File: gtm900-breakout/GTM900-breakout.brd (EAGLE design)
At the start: 70 x 70 mm, 45 parts, among them K1 694108106102, T1 BC847, U1 FH12A-40S-0.5SH(55), U2 FH12A-40S-0.5SH(55), U3 MCP1827T-ADJE/ET

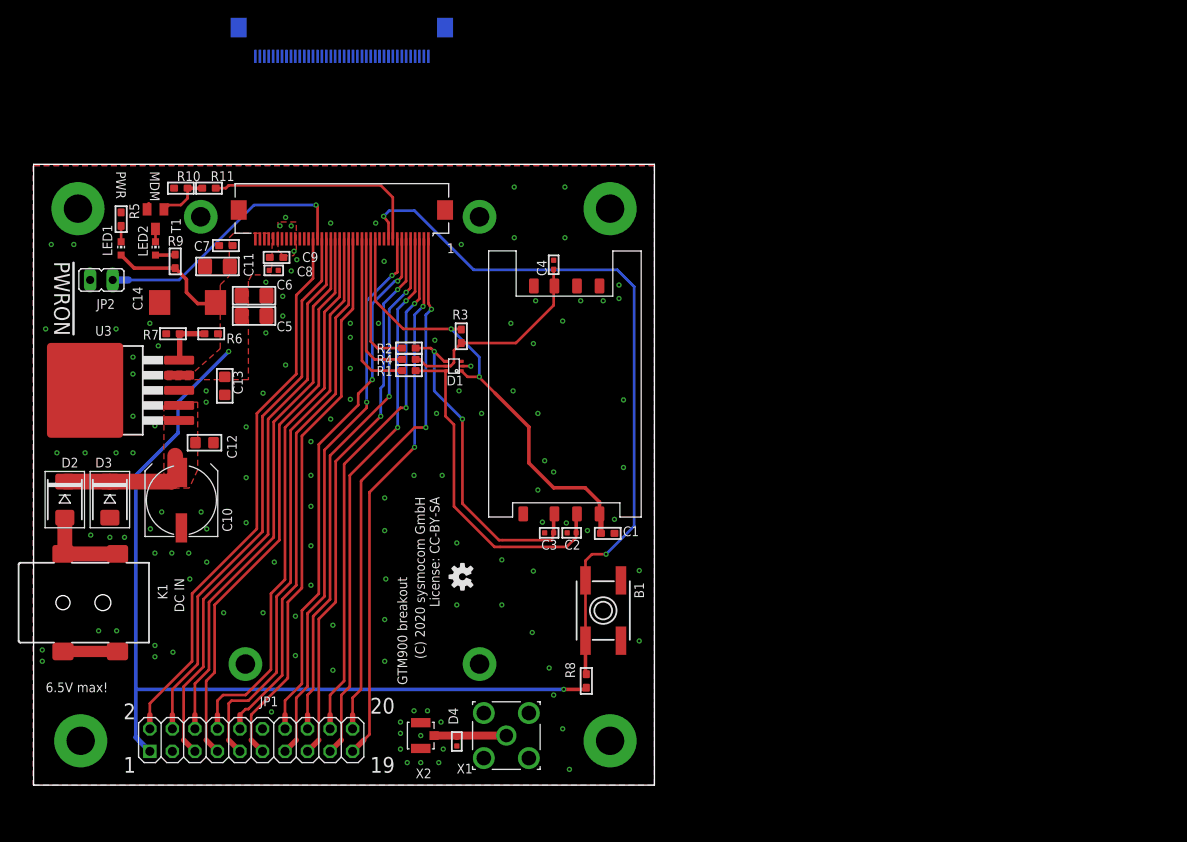
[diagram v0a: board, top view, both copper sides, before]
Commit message: gtm900: added CP2105 and 3.5mm TRRS audio jack, remv'd aux conn
adds to OS#4030
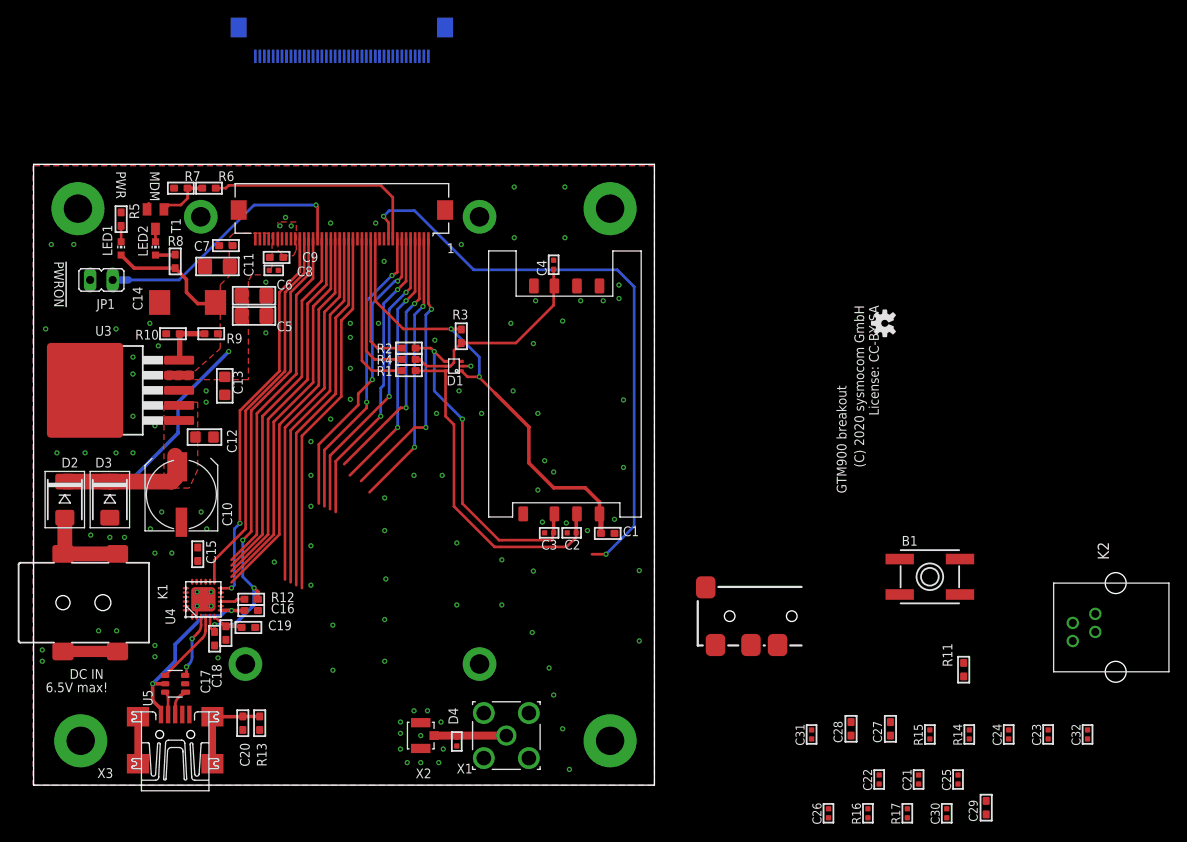
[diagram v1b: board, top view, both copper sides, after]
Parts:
- removed JP2: (no value), jumper:JP1
- added C15, C19: 4.7u, rc-sysmocom:_0603
- added C16: 1u, rc-sysmocom:_0603
- added C17, C18, C20, C27, C28: 100n, rc-sysmocom:_0603
- added C21, C22, C23, C24, C25, C26, C30, C31, C32: 33p, rc-sysmocom:_0402
- added C29: 22u, rc-sysmocom:_0603
- added J1: SJ2-3574A, SparkFun-Connectors:AUDIO-JACK-TRRS-SMD
- added K2: 615004143821, Wuerth_Elektronik_eiCan_Communication_Connectors_v6_20150113:615004143821
- added R12: 4.7k, rc-sysmocom:_0603@1
- added R13: 1M, rc-sysmocom:_0603@1
- added R14, R17: 100, rc-sysmocom:_0402@1
- added R15, R16: 2.2k, rc-sysmocom:_0402@1
- added U4: CP2105-GM, usb-uart:QFN24_4X4
- added U5: IP4234CZ6, laforge:TSOP-6
- added X3: MINI-USB-SHIELD-UX60-MB-5ST, con-hirose:UX60-MB-5ST
- JP1: device laforge:2X10 -> jumper:JP1
- R1, R10, R2, R3, R4, R5, R7: device rc-sysmocom:_0603 -> rc-sysmocom:_0603@1
- R11: value 22k -> 15k; device rc-sysmocom:_0603 -> rc-sysmocom:_0603@1
- R6: value 200k -> 22k; device rc-sysmocom:_0603 -> rc-sysmocom:_0603@1
- R8: value 15k -> 330; device rc-sysmocom:_0603 -> rc-sysmocom:_0603@1
- R9: value 330 -> 200k; device rc-sysmocom:_0603 -> rc-sysmocom:_0603@1
- moved R11 100.9 mm to (78.7, 13.0), turned to 90 degrees
- moved R8 66.2 mm to (-10.2, 59.1)
- moved U$1 55.5 mm to (69.8, 52.1)
- moved JP1 54.6 mm to (-18.5, 57.0), turned to 90 degrees
- moved B1 37.0 mm to (74.9, 23.5), turned to 0 degrees
- moved R10 16.4 mm to (-10.4, 50.9)
- moved R7 16.4 mm to (-9.53, 67.3)
- moved R6 16.4 mm to (-6.35, 67.3), turned to 180 degrees
- moved R9 9.12 mm to (-6.10, 50.9), turned to 0 degrees
- moved C12 0.64 mm to (-6.86, 39.2)
- moved C10 0.63 mm to (-9.46, 32.8)
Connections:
- removed net N$24: JP1.12
- new net N$11: C20.2, R13.2, X3.M1, X3.M2, X3.M3, X3.M4
- new net N$12: R12.1, U4.9
- new net N$14: C15.2, U4.16
- new net N$15: C27.2, C31.1, J1.RING2, R15.2
- new net N$16: C29.1, C30.1, R14.2, R15.1
- new net N$17: C29.2, C30.2, R16.2, R17.1
- new net N$20: C28.2, C31.2, J1.TIP, R16.1
- new net USB_DN: U4.4, U5.4
- new net USB_DP: U4.3, U5.3
- new net USB_VBUS: C16.1, U4.7, U4.8, U5.5, X3.1
- new net VDD_3V45: C18.1, C19.1, U4.6
- new net _USB_DN: U5.6, X3.2
- new net _USB_DP: U5.1, X3.3
- net !RST: now also R11.2; no longer R8.2
- net ADC: no longer JP1.2
- net AUXI+: no longer JP1.19
- net AUXI-: no longer JP1.20
- net AUXO+: no longer JP1.13
- net AUXO-: no longer JP1.14
- net EAR+: now also C23.1, C26.1, C32.2, J1.RING1; no longer JP1.15
- net EAR-: now also C24.2, C26.2, C32.1, J1.EARTH; no longer JP1.16
- net GND: now also C15.1, C16.2, C17.1, C18.2, C19.2, C20.1, C21.2, C22.1, C23.2, C24.1, JP1.2, R13.1, R17.2, U4.2, U4.25, U5.2, X3.5; no longer JP1.3, JP2.2
- net LPG: now also R6.1; no longer R11.1
- net MIC+: now also C21.1, C25.1, C27.1; no longer JP1.17
- net MIC-: now also C22.2, C25.2, C28.1; no longer JP1.18
- net N$2: now also R8.2; no longer R9.2
- net N$5: now also R6.2, R7.1; no longer R10.1, R11.2
- net N$6: now also R10.1, R9.1; no longer R6.1, R7.1
- net PWON: now also JP1.1; no longer JP2.1
- net RXD2: now also U4.12
- net TXD2: now also U4.13
- net UART_CTS: now also U4.18; no longer JP1.8
- net UART_DCD: now also U4.24; no longer JP1.11
- net UART_DSR: now also U4.22; no longer JP1.4
- net UART_DTR: now also U4.23; no longer JP1.10
- net UART_RI: now also U4.1; no longer JP1.5
- net UART_RTS: now also U4.19; no longer JP1.9
- net UART_RXD: now also U4.20; no longer JP1.6
- net UART_TXD: now also U4.21; no longer JP1.7
- net VCC: now also R11.1, R9.2; no longer JP1.1, R6.2, R9.1
- net VDD: now also C17.2, R12.2, R14.1, U4.5
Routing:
- net VCC: track 114.8 -> 32.1 mm, vias 2 -> 1
- net VDD: track 0.00 -> 54.4 mm, vias 0 -> 3
- net RXD2: track 0.00 -> 43.8 mm, vias 0 -> 2
- net TXD2: track 0.00 -> 42.9 mm
- net MIC+: track 61.8 -> 29.7 mm
- net MIC-: track 59.8 -> 29.3 mm
- net AUXI+: track 61.1 -> 31.1 mm
- net AUXO+: track 63.1 -> 33.7 mm
- net AUXI-: track 59.8 -> 31.4 mm
- net EAR+: track 62.4 -> 34.1 mm
- net AUXO-: track 60.9 -> 33.9 mm
- net EAR-: track 60.1 -> 34.2 mm
- net UART_RTS: track 64.8 -> 41.2 mm
- net UART_RI: track 65.0 -> 41.9 mm
- net ADC: track 62.9 -> 40.0 mm
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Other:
- board text removed: "19"
- board text removed: "2"
- board text removed: "20"

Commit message: gtm900-bo: hopefully incorporating all we discussed last weeks
see OS#4030
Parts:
- removed K2: 615004143821, Wuerth_Elektronik_eiCan_Communication_Connectors_v6_20150113:615004143821
- removed U$1: (no value), SparkFun-Aesthetics:OSHW-LOGO-S
- added B2: (no value), microbuilder:EVQ-Q2
- added C33, C34: 33p, rc-sysmocom:_0402
- added D5: PESD5V0UBV, laforge:SOT666
- added JP2: (no value), microbuilder:1X04_ROUND_76
- added LOGO3: OSHW-LOGOS-COPPER, SparkFun-Aesthetics:OSHW-LOGO-S_COPPER
- added R18, R20, R21: 22k, rc-sysmocom:_0603@1
- added R19: 330, rc-sysmocom:_0603@1
- added R22: DNP, rc-sysmocom:_0603@1
- added R23: 1k, rc-sysmocom:_0603@1
- added R24: 4.7k, rc-sysmocom:_0603@1
- added R25: 1M, rc-sysmocom:_0603@1
- added R26: 0, rc-sysmocom:_0603@1
- added T2, T3, T4: BC847, transistor:SOT23-BEC
- added TP1, TP2, TP3, TP4, TP5: TPTP10R, testpad:TP10R
- added U$3: (no value), SparkFun-Aesthetics:OSHW-LOGO-S
- added U6: IP4234CZ6, laforge:TSOP-6
- added X4: MINI-USB-SHIELD-UX60-MB-5ST, con-hirose:UX60-MB-5ST
- C10: value 470u -> 100u; device rcl:UD-8X10_NICHICON -> rc-sysmocom:1206
- C11: value 100u -> 470u; device rc-sysmocom:1206 -> rcl:UD-8X10_NICHICON
- C13: value 10u -> 100n; device rc-sysmocom:_0805 -> rc-sysmocom:_0603
- C14: value DNP -> 1u; device rcl:SMC_E -> rc-sysmocom:_0603
- C15: value 4.7u -> 1u
- C16: value 1u -> 10u; device rc-sysmocom:_0603 -> rc-sysmocom:_0805
- C17: value 100n -> DNP; device rc-sysmocom:_0603 -> rcl:SMC_E
- C20: value 100n -> 1u
- C21, C22, C24: value 33p -> 100n; device rc-sysmocom:_0402 -> rc-sysmocom:_0603
- C23: value 33p -> 4.7u; device rc-sysmocom:_0402 -> rc-sysmocom:_0603
- C27, C28: value 100n -> 33p; device rc-sysmocom:_0603 -> rc-sysmocom:_0402
- C29: value 22u -> 33p; device rc-sysmocom:_0603 -> rc-sysmocom:_0402
- C31, C32: value 33p -> 10u; device rc-sysmocom:_0402 -> rc-sysmocom:_0805
- J1: value SJ2-3574A -> AUDIO-JACK3
- MDM1: value GTM900-B -> GTM900-BM2-SPACER; device GTM900:GTM900 -> GTM900:GTM900-WRTHSPACER
- R1: value 47 -> 15k
- R11: value 15k -> 4.7k
- R12: value 4.7k -> DNP
- R13: value 1M -> 1k
- R14: value 100 -> 0; device rc-sysmocom:_0402@1 -> rc-sysmocom:_0603@1
- R15: value 2.2k -> 200k; device rc-sysmocom:_0402@1 -> rc-sysmocom:_0603@1
- R16: value 2.2k -> 22k; device rc-sysmocom:_0402@1 -> rc-sysmocom:_0603@1
- R17: value 100 -> 22k; device rc-sysmocom:_0402@1 -> rc-sysmocom:_0603@1
- R3: value 15k -> 47
- R4: value 47 -> 4.7k
- R5: value 330 -> 47k
- R6: value 22k -> 330
- R8: value 330 -> 22k
- R9: value 200k -> 22k
- U4: value CP2105-GM -> MIC5366; device usb-uart:QFN24_4X4 -> ldo:SC70-5
- U5: value IP4234CZ6 -> CP2105-GM; device laforge:TSOP-6 -> usb-uart:QFN24_4X4
- X1: device laforge:SMA-F-S-TH -> laforge:1X03
- X2: device laforge:HRS_UFL -> laforge:SMA-F-S-TH
- X3: value MINI-USB-SHIELD-UX60-MB-5ST -> (none); device con-hirose:UX60-MB-5ST -> laforge:HRS_UFL
- moved R17 105.7 mm to (-6.35, 67.3), turned to 180 degrees
- moved R16 95.2 mm to (-10.4, 50.9), turned to 180 degrees
- moved R15 92.8 mm to (-6.10, 50.9), turned to 0 degrees
- moved C24 89.6 mm to (-5.71, 10.2), turned to 0 degrees
- moved C23 89.3 mm to (0.00, 19.1), turned to 270 degrees
- moved C32 84.1 mm to (9.53, 18.4)
- moved C25 84.0 mm to (14.3, 55.2), turned to 135 degrees
- moved C29 83.9 mm to (18.0, 52.6), turned to 0 degrees
- moved C30 83.3 mm to (15.9, 53.7), turned to 315 degrees
- moved C21 79.3 mm to (-2.86, 21.3), turned to 0 degrees
- moved T1 73.0 mm to (40.0, 13.0), turned to 0 degrees
- moved C22 72.9 mm to (-1.27, 19.1), turned to 270 degrees
- moved R7 71.8 mm to (35.6, 11.4), turned to 270 degrees
- moved C28 69.0 mm to (14.9, 52.7), turned to 315 degrees
- moved R14 66.7 mm to (17.1, 29.8)
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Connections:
- removed net N$20: C28.2, C31.2, J1.TIP, R16.1
- removed net PWON: JP1.1, U1.26, U2.15
- removed net USB_DN: U4.4, U5.4
- removed net USB_DP: U4.3, U5.3
- removed net _USIM_IO: R4.1, U1.15, U2.26
- new net !PWON: C18.1, JP1.1, R22.2, R23.1, T4.C, U1.26, U2.15
- new net GPIO.0_ECI/DTR_ECI: R14.2, R20.1, U5.15
- new net GPIO.1_ECI/DSR_ECI: R7.1, U5.14
- new net N$10: R4.1, SIM1.82
- new net N$18: R11.1, R14.1, T2.C
- new net N$21: B1.A, B1.A', R13.2
- new net N$7: R10.1, R8.2, T2.B
- new net N$8: C32.1, C34.2, J1.2, J1.3
- new net N$9: B2.A, B2.A', R23.2
- new net USB_D_N: U5.4, U6.4
- new net USB_D_P: U5.3, U6.3
- new net VIO_2V8: C15.2, C21.2, R11.2, R12.1, R22.1, U4.5, U5.5
- net !RST: now also C13.1, R12.2, R13.1, T1.C; no longer B1.A, B1.A', R11.2
- net ADC: now also X1.1
- net AUXI+: now also TP3.TP
- net AUXI-: now also TP5.TP
- net AUXO+: now also TP2.TP
- net AUXO-: now also TP4.TP
- net EAR+: now also C25.2, D5.3, JP2.3; no longer C23.1, J1.RING1
- net EAR-: now also C25.1, C27.2, D5.1, JP2.4, R26.2; no longer C24.2, C26.2, C32.1, J1.EARTH
- net GND: now also B2.B, B2.B', C10.1, C11.-, C13.2, C14.1, C16.1, C17.-, C19.1, C20.2, C21.1, C22.2, C26.2, C27.1, C28.2, C29.2, C31.2, C33.2, C34.1, D5.2, J1.4, MDM1.1, MDM1.2, MDM1.3, MDM1.4, R16.2, R18.2, R21.2, R25.1, R26.1, R6.1, R9.2, T2.E, T3.E, T4.E, U5.25, U6.2, X1.3, X2.G1, X2.G2, X2.G3, X2.G4, X3.GND@1, X3.GND@2, X4.5; no longer C10.-, C11.1, C13.1, C14.-, C16.2, C17.1, C19.2, C20.1, C21.2, C22.1, MDM1.P$1, MDM1.P$2, MDM1.P$3, MDM1.P$4, R13.1, R17.2, R7.2, U4.25, X1.G1, X1.G2, X1.G3, X1.G4, X2.GND@1, X2.GND@2, X3.5
- net LDO_IN: now also C11.+; no longer C10.+
- net LPG: now also R17.1; no longer R6.1
- net MIC+: now also C28.1, C30.1, C33.1, D5.4, J1.1, JP2.1; no longer C21.1, C25.1, C27.1
- net MIC-: now also C29.1, C30.2, C31.1, D5.5, JP2.2; no longer C22.2, C25.2, C28.1
- net N$1: now also R6.2; no longer R5.2
- net N$11: now also C24.2, R25.2, X4.M1, X4.M2, X4.M3, X4.M4; no longer C20.2, R13.2, X3.M1, X3.M2, X3.M3, X3.M4
- net N$12: now also R24.1, U5.9; no longer R12.1, U4.9
- net N$13: now also X2.C, X3.SIG; no longer X1.C, X2.SIG
- net N$14: now also C19.2, U5.16; no longer C15.2, U4.16
- net N$15: now also R4.2; no longer C27.2, C31.1, J1.RING2, R15.2
- net N$16: now also R20.2, R21.1, T4.B; no longer C29.1, C30.1, R14.2, R15.1
- net N$17: now also R7.2, R9.1, T1.B; no longer C29.2, C30.2, R16.2, R17.1
- net N$2: now also R19.2; no longer R8.2
- net N$3: now also T3.C; no longer T1.C
- net N$5: now also R17.2, R18.1, T3.B; no longer R6.2, R7.1, T1.B
- net N$6: now also R15.1, R16.1; no longer R10.1, R9.1
- net RXD2: now also U5.12; no longer U4.12
- net TXD2: now also U5.13; no longer U4.13
- net UART_CTS: now also U5.18; no longer U4.18
- net UART_DCD: now also U5.24; no longer U4.24
- net UART_DSR: now also U5.22; no longer U4.22
- net UART_DTR: now also R8.1, U5.23; no longer U4.23
- net UART_RI: now also U5.1; no longer U4.1
- net UART_RTS: now also U5.19; no longer U4.19
- net UART_RXD: now also U5.20; no longer U4.20
- net UART_TXD: now also U5.21; no longer U4.21
- net USB_VBUS: now also C14.2, C20.1, U4.1, U4.3, U5.7, U5.8, U6.5, X4.1; no longer C16.1, U4.7, U4.8, U5.5, X3.1
- net USIM_CD: now also R5.2, SIM1.81
- net USIM_CLK: now also R3.2; no longer R2.2
- net USIM_IO: now also R1.1, U1.15, U2.26; no longer R3.1, R4.2
- net USIM_RESET: now also R2.2; no longer R1.2
- net USIM_VCC: now also R1.2; no longer R3.2
- net VBACKUP: now also X1.2
- net VCC: now also C10.2, C16.2, C17.+, R15.2, R19.1; no longer C11.2, C13.2, C14.+, R11.1, R8.1, R9.2
- net VDD: now also R24.2; no longer C17.2, R12.2, R14.1, U4.5
- net VDD_3V45: now also C22.1, C23.1, TP1.TP, U5.6; no longer C18.1, C19.1, U4.6
- net _USB_DN: now also U6.6, X4.2; no longer U5.6, X3.2
- net _USB_DP: now also U6.1, X4.3; no longer U5.1, X3.3
- net _USIM_CLK: now also R3.1; no longer R2.1
- net _USIM_RESET: now also R2.1; no longer R1.1
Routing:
- net VIO_2V8: track 0.00 -> 83.5 mm, vias 0 -> 3
- net !PWON: track 0.00 -> 79.1 mm, vias 0 -> 2
- net USIM_CD: track 0.00 -> 45.7 mm, vias 0 -> 3
- net GPIO.1_ECI/DSR_ECI: track 0.00 -> 35.3 mm, vias 0 -> 2
- net PWON: track 30.3 -> 0.00 mm, vias 1 -> 0
- net MIC+: track 29.7 -> 57.9 mm, vias 2 -> 1
- net VBACKUP: track 0.00 -> 26.4 mm, vias 0 -> 1
- net GPIO.0_ECI/DTR_ECI: track 0.00 -> 21.6 mm, vias 0 -> 2
- net USB_VBUS: track 21.8 -> 43.4 mm, vias 2 -> 3
- net USB_D_N: track 0.00 -> 20.0 mm
- net USIM_IO: track 23.7 -> 43.3 mm
- net USB_D_P: track 0.00 -> 19.6 mm, vias 0 -> 2
- net VCC: track 32.1 -> 13.8 mm, vias 1 -> 0
- net _USIM_IO: track 17.1 -> 0.00 mm
- net AUXO-: track 33.9 -> 18.4 mm
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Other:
- board text added: "PWON"
- board text added: "RESET"

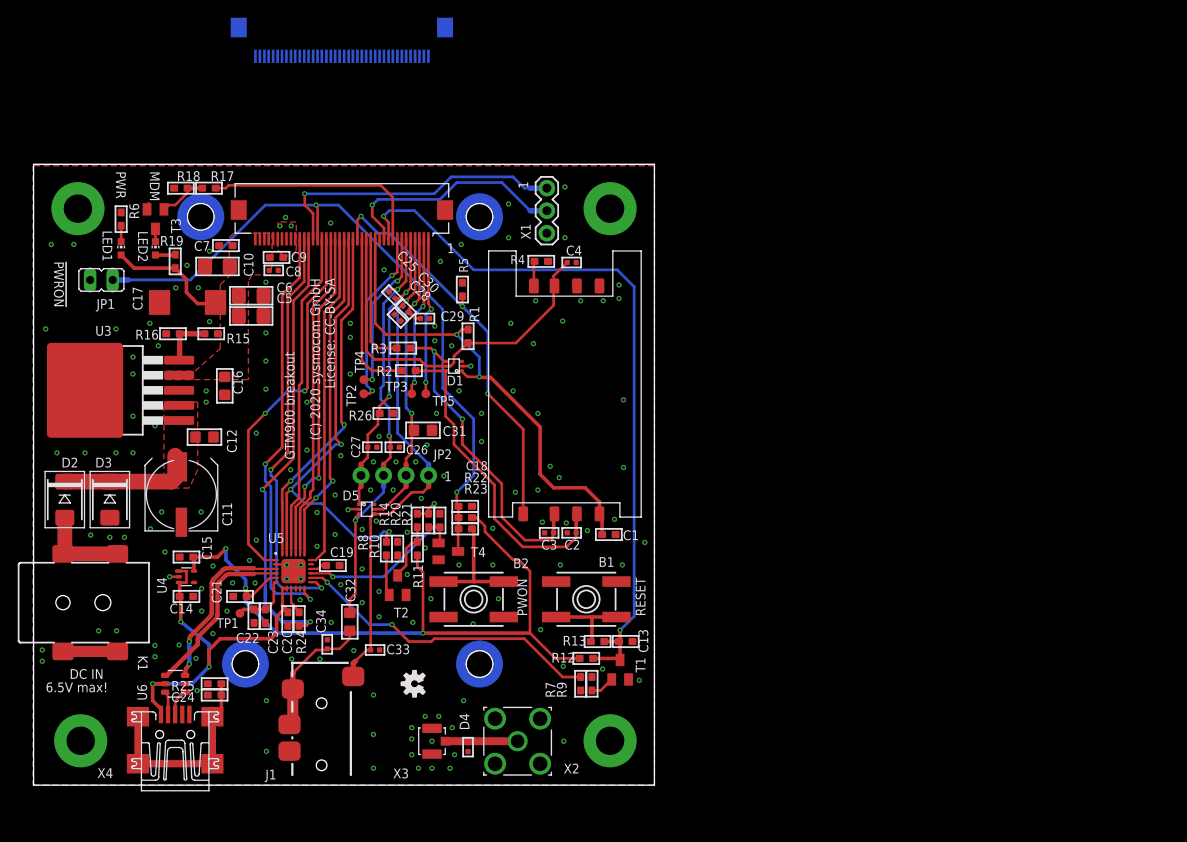
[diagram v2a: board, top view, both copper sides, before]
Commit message: gtm900-bo: routing done, no airwires left, mirrored FPC removed
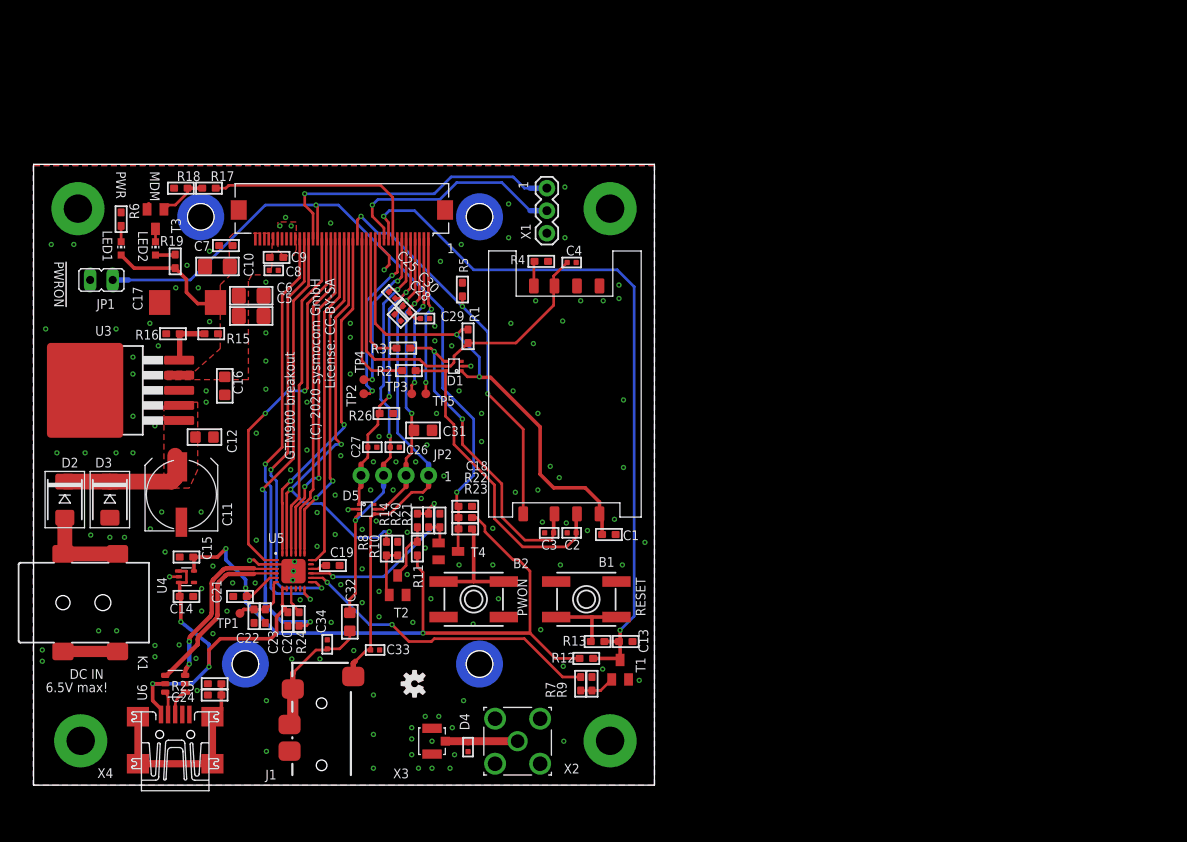
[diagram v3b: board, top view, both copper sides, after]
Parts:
- removed U2: FH12A-40S-0.5SH(55), FH12A-40S-0.5SH(55):HIROSE_FH12A-40S-0.5SH(55)
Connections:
- removed net USIM_GND: U1.12
- net !PWON: no longer U2.15
- net !RST: no longer U2.31
- net ADC: no longer U2.14
- net AUXI+: no longer U2.39
- net AUXI-: no longer U2.40
- net AUXO+: no longer U2.33
- net AUXO-: no longer U2.34
- net EAR+: no longer U2.35
- net EAR-: no longer U2.36
- net GND: now also U1.12; no longer U2.10, U2.29, U2.6, U2.7, U2.8, U2.9
- net LPG: no longer U2.32
- net MIC+: no longer U2.37
- net MIC-: no longer U2.38
- net RXD2: no longer U2.11
- net TXD2: no longer U2.12
- net UART_CTS: no longer U2.20
- net UART_DCD: no longer U2.23
- net UART_DSR: no longer U2.16
- net UART_DTR: no longer U2.22
- net UART_RI: no longer U2.17
- net UART_RTS: no longer U2.21
- net UART_RXD: no longer U2.18
- net UART_TXD: no longer U2.19
- net USIM_CD: no longer U2.24
- net USIM_IO: no longer U2.26
- net USIM_VCC: no longer U2.28
- net VBACKUP: no longer U2.30
- net VCC: no longer U2.1, U2.2, U2.3, U2.4, U2.5
- net VDD: no longer U2.13
- net _USIM_CLK: no longer U2.27
- net _USIM_RESET: no longer U2.25
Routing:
- net GND: track 11.8 -> 19.2 mm, vias 168 -> 167
- net MIC+: track 57.9 -> 59.3 mm
- net N$7: track 4.60 -> 5.87 mm
- net N$17: track 2.74 -> 4.01 mm
